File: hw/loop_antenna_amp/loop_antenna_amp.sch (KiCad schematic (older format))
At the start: 71 parts

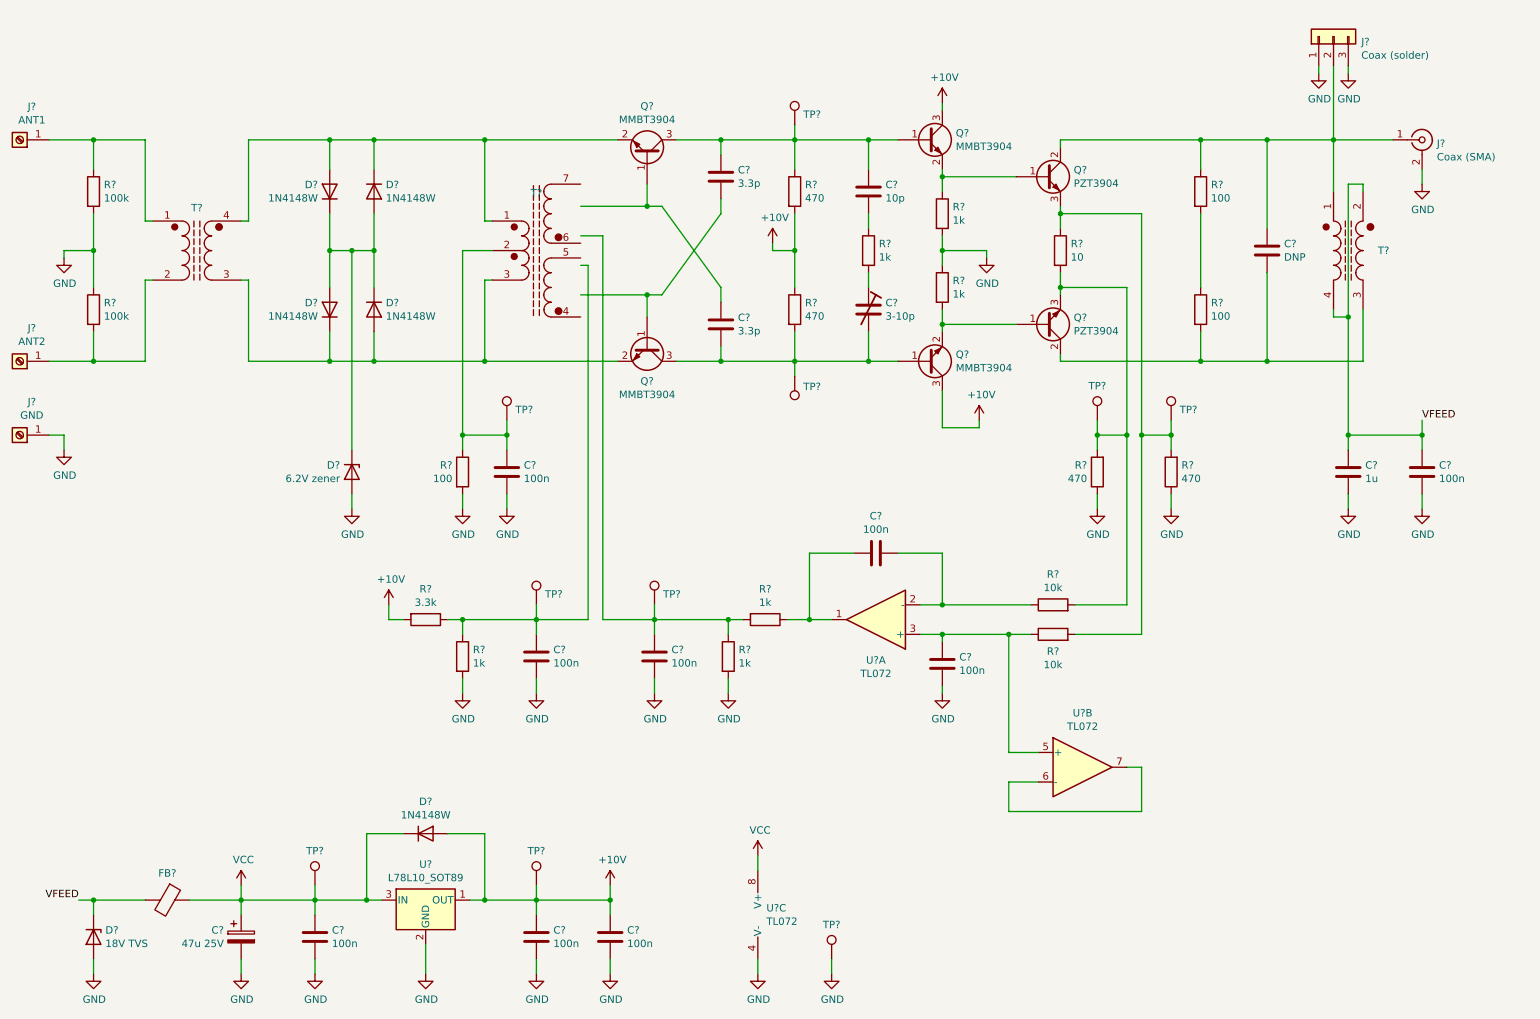
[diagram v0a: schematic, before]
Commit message: Loop antenna: annotate schematic
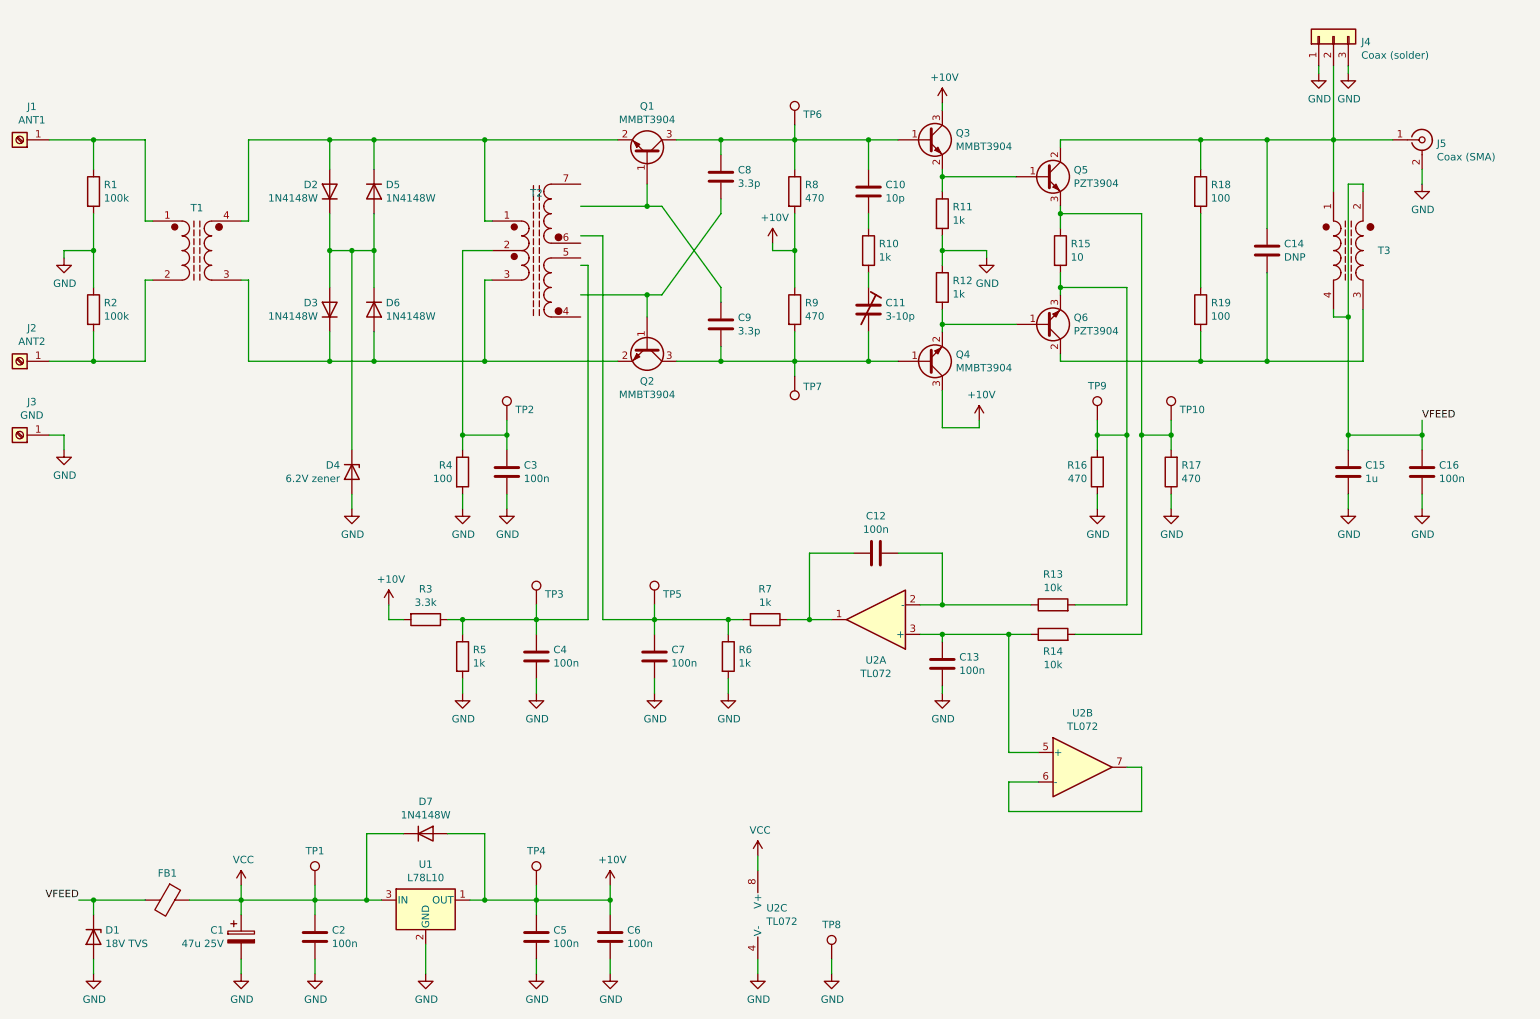
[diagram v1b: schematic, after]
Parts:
- U1: renamed from U?; value L78L10_SOT89 -> L78L10
- gave numbers to parts that had none: 68

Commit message: Loop antenna: add comments to schematic
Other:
- note added: "Adjust C11 to achieve frequency response drop\nof -3dB @ 35-40 MHz without excessive peaking.\nReplace C8, C9 if needed."
- note added: "DC bias regulator"
- note added: "DC-biased antenna feed\npower supply"
- note added: "Transformer T1:\n Fair-Rite 5943004901 toroid\n 5 turns of RG174\n\nTransformer T2:\n Fair-Rite 2843000202 core (BN-43-202)\n 0.3mm magnetic copper wire\n 1-2: 1 turn\n 2-3: 1 turn\n 4-5: 8 turns\n 6-7: 8 turns\n\nTransformer T3:\n Fair-Rite 2843000202 core (BN-43-202)\n 10 turns of twisted pair made from\n 0.3mm magnetic copper wire\n"
- note added: "Unused opamp"
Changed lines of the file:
@@
 Wire Wire Line
 	6500 7050 6500 7150
+Text Notes 1000 5400 0    50   ~ 0
+Transformer T1:\n  Fair-Rite 5943004901 toroid\n  5 turns of RG174\n\nTransformer T2:\n  Fair-Rite 2843000202 core (BN-43-202)\n  0.3mm magnetic copper wire\n  1-2: 1 turn\n  2-3: 1 turn\n  4-5: 8 turns\n  6-7: 8 turns\n\nTransformer T3:\n  Fair-Rite 2843000202 core (BN-43-202)\n  10 turns of twisted pair made from\n  0.3mm magnetic copper wire\n
+Text Notes 5000 1000 0    50   ~ 0
+Adjust C11 to achieve frequency response drop\nof -3dB @ 35-40 MHz without excessive peaking.\nReplace C8, C9 if needed.
+Text Notes 6500 3900 0    50   ~ 0
+DC bias regulator
+Text Notes 8500 5500 0    50   ~ 0
+Unused opamp
+Text Notes 1000 6300 0    50   ~ 0
+DC-biased antenna feed\npower supply
 $EndSCHEMATC

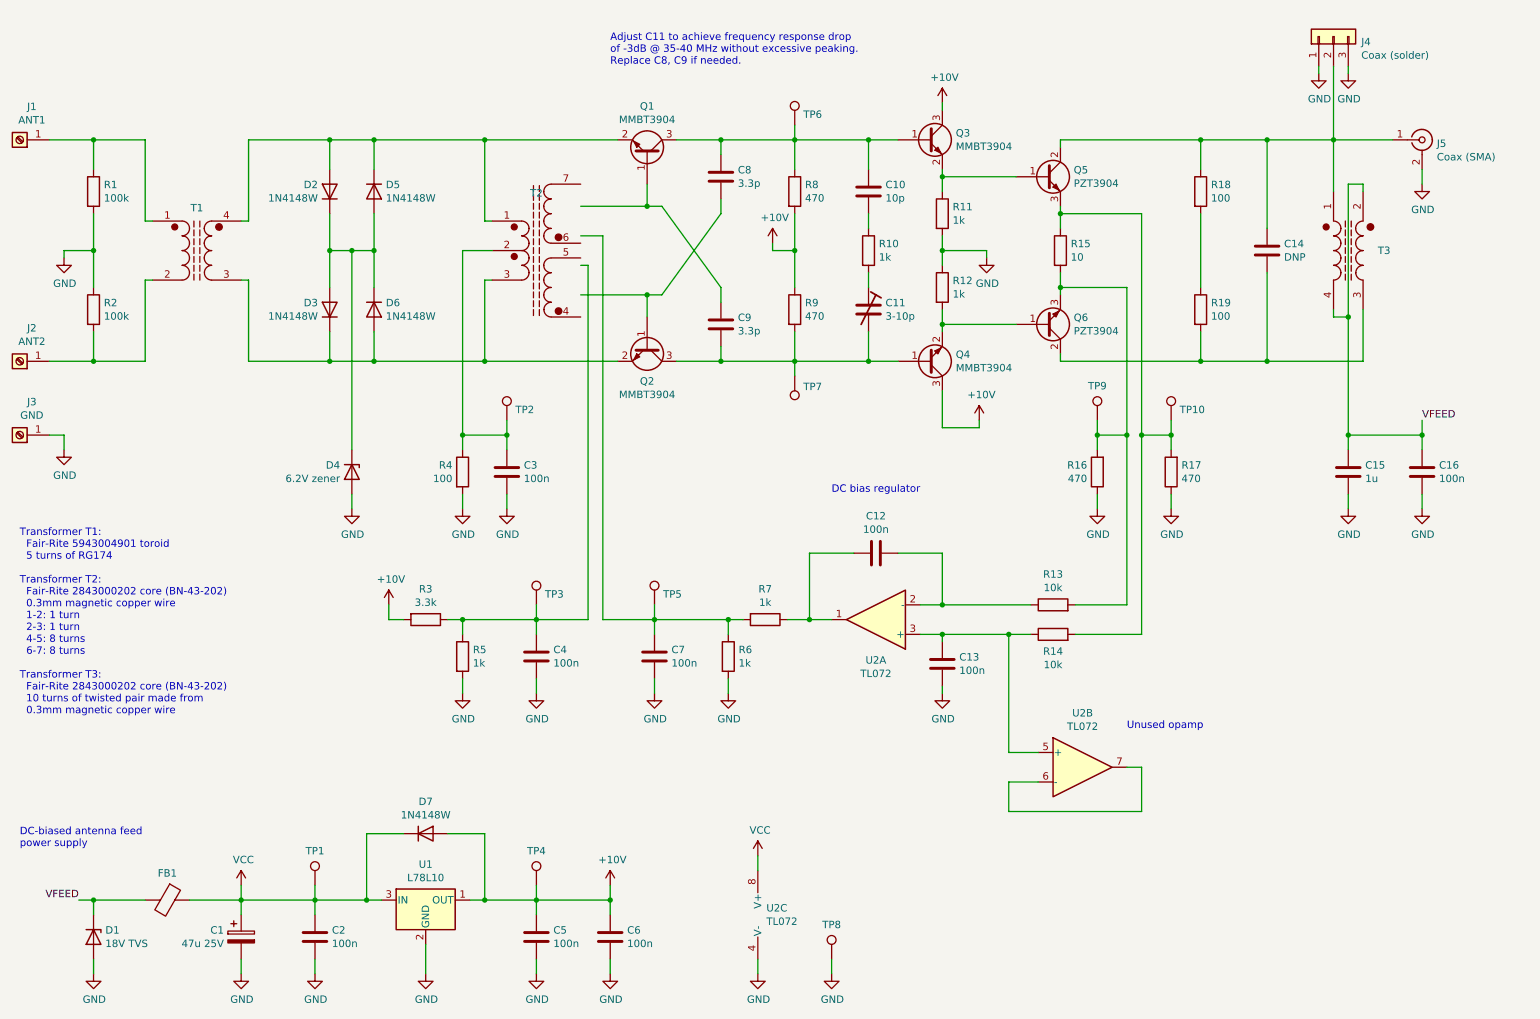
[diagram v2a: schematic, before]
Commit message: Loop antenna: redraw transformer, add protection diodes based on LTSpice simulation
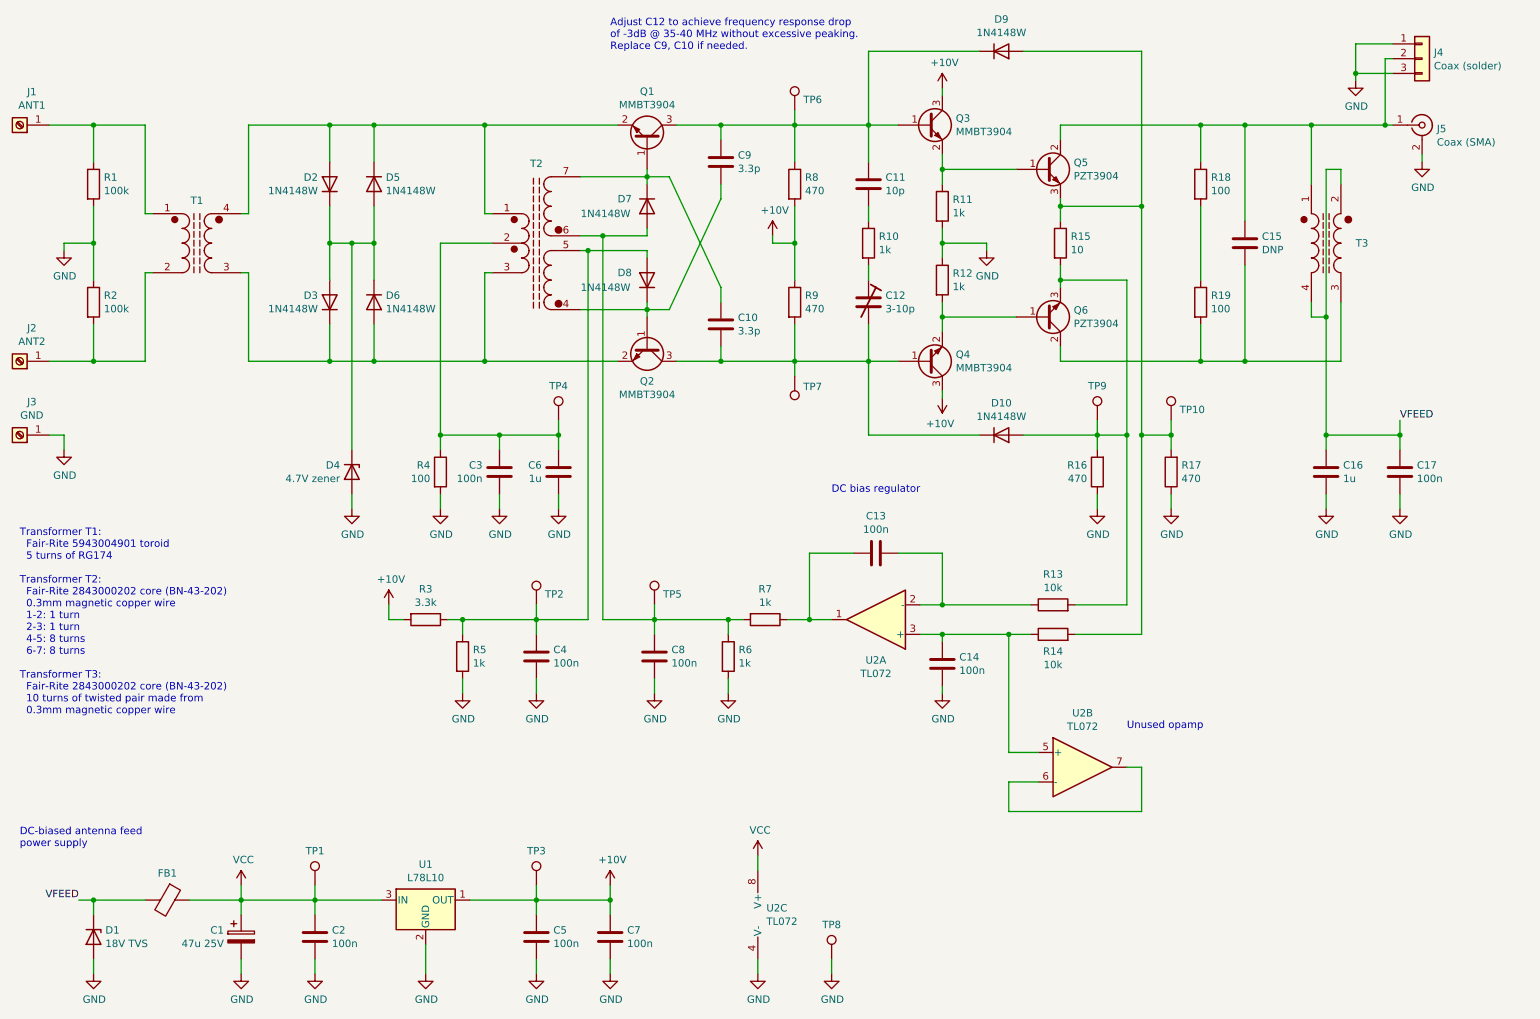
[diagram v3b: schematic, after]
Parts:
- added C6: 1u, symbol Device:C
- added D10, D8, D9: 1N4148W, Diode_SMD:D_SOD-123, symbol Diode:1N4148W
- D4: value 6.2V zener -> 4.7V zener
- renumbered C9 to C10, C10 to C11, C11 to C12, C12 to C13, C13 to C14, C14 to C15, C15 to C16, C16 to C17, C6 to C7, C7 to C8, C8 to C9, TP3 to TP2, TP4 to TP3, TP2 to TP4
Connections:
- net +10V: no longer D7.2 (A)
- net GND: now also C6.2
- net VCC: no longer D7.1 (K)
- net at C3.1, R4.1, T2.2 (AB)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: now also C6.1
- net at T2.4 (BA): now also C9.1, Q2.1 (B), D8.1 (K)
- net at T2.5 (BB): now also C4.1, R3.1, R5.1, TP2.1, D8.2 (A)
- net at T2.6 (CA): now also C8.1, D7.2 (A), R6.1, R7.2, TP5.1
- net at T2.7 (CB): now also C10.2, D7.1 (K), Q1.1 (B)
- net at C11.1, C9.2, Q1.3 (C)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: now also D9.1 (K)
- net at C10.1, C12.2, Q2.3 (C)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: now also D10.1 (K)
- net at Q5.3 (E), R14.2, R15.1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: now also D9.2 (A)
- net at Q6.3 (E), R13.2, R15.2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: now also D10.2 (A)
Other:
- note added: "Adjust C12 to achieve frequency response drop\nof -3dB @ 35-40 MHz without excessive peaking.\nReplace C9, C10 if needed."
- note removed: "Adjust C11 to achieve frequency response drop\nof -3dB @ 35-40 MHz without excessive peaking.\nReplace C8, C9 if needed."
- moved on the sheet: C11, C12, C15, C16, C17, C3, C9, D2, D3, D5, D6, J1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

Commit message: Loop antenna: add custom footprints, assign footprints
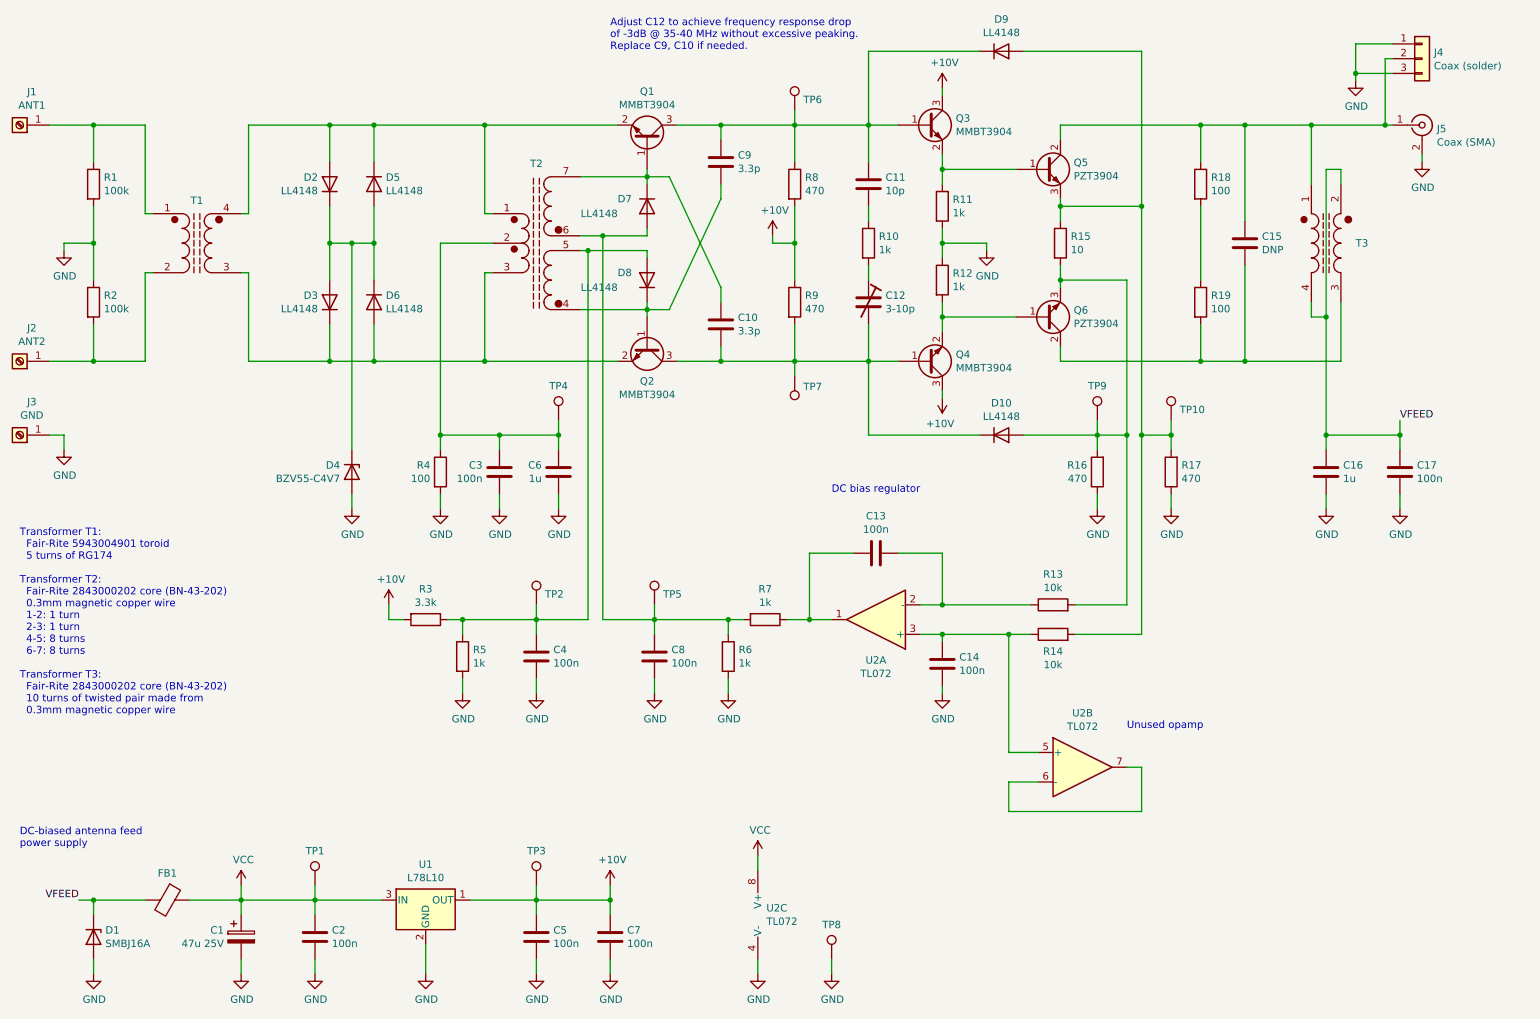
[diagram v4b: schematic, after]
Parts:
- C1: footprint (none) -> Capacitor_THT:CP_Radial_D5.0mm_P2.00mm
- C10, C11, C15, C17, C2, C3, C4, C5, C6, C7, C8, C9: footprint (none) -> Capacitor_SMD:C_0805_2012Metric_Pad1.15x1.40mm_HandSolder
- C12: footprint (none) -> Capacitor_SMD:C_Trimmer_Murata_TZB4-A
- C13, C14: footprint (none) -> Capacitor_THT:C_Rect_L7.0mm_W2.5mm_P5.00mm
- C16: footprint (none) -> Capacitor_THT:C_Rect_L7.0mm_W4.5mm_P5.00mm
- D1: value 18V TVS -> SMBJ16A; footprint (none) -> Diode_SMD:D_SMB_Handsoldering
- D10, D2, D3, D5, D6, D7, D8, D9: value 1N4148W -> LL4148; footprint Diode_SMD:D_SOD-123 -> Diode_SMD:D_MiniMELF
- D4: value 4.7V zener -> BZV55-C4V7; footprint (none) -> Diode_SMD:D_MiniMELF
- FB1: footprint (none) -> Inductor_SMD:L_1206_3216Metric_Pad1.42x1.75mm_HandSolder
- J1, J2, J3: footprint (none) -> local_footprints:Keystone_7771_ScrewTerminal
- J5: footprint (none) -> Connector_Coaxial:SMA_Amphenol_132134_Vertical
- R1, R10, R11, R12, R13, R14, R15, R16, R17, R18, R19, R2, R3, R4, R5, R6, R7, R8, R9: footprint (none) -> Resistor_SMD:R_0805_2012Metric_Pad1.15x1.40mm_HandSolder
- T1: footprint (none) -> local_footprints:FairRite_5943004901_Standing
- T2: footprint (none) -> local_footprints:BN_43_202_Trafo1SP2S
- T3: footprint (none) -> local_footprints:BN_43_202_Trafo1P1S
- TP1, TP10, TP2, TP3, TP4, TP5, TP6, TP7, TP9: footprint (none) -> TestPoint:TestPoint_THTPad_D1.0mm_Drill0.5mm
- TP8: footprint (none) -> TestPoint:TestPoint_THTPad_D2.5mm_Drill1.2mm
- U2: footprint (none) -> Package_SO:SO-8_3.9x4.9mm_P1.27mm
